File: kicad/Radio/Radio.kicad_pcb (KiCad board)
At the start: 2 copper layers, 129 x 99.5 mm, 44 parts, among them J1 PCB_SMA, J2 Conn_01x02, J3 Audio_Jack, Q1 MOSFET-NCH-AO3404A, Q2 MOSFET-NCH-AO3404A, SW1 Rotary_Encoder_Switch, T1 6:31, T2 31:6, T3 T50_SPLITTER, U1 LM7805_TO220, U2 FST3253, U3 LM358, U4 si5351, U5 TINYPico

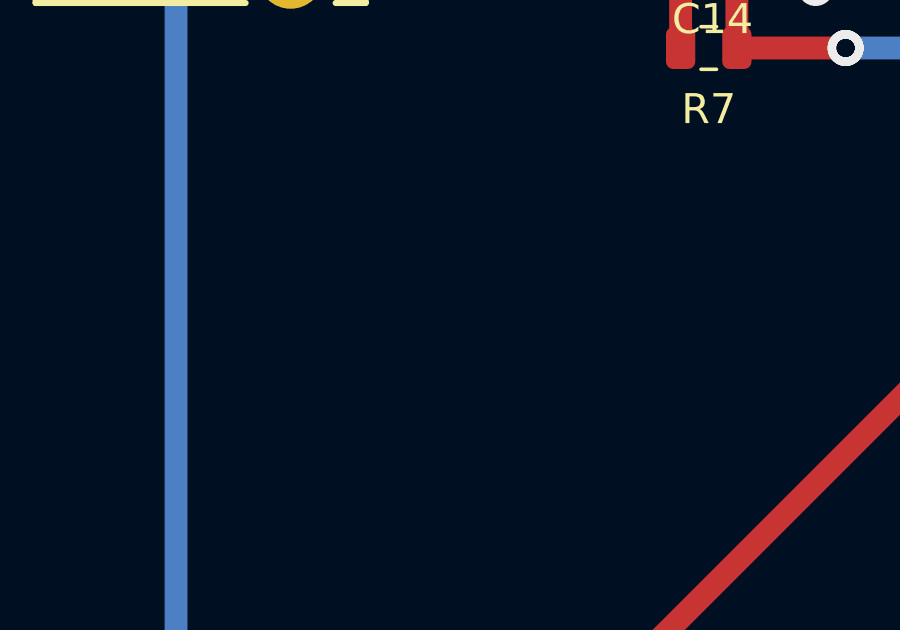
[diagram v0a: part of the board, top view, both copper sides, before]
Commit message: fixing cap placement
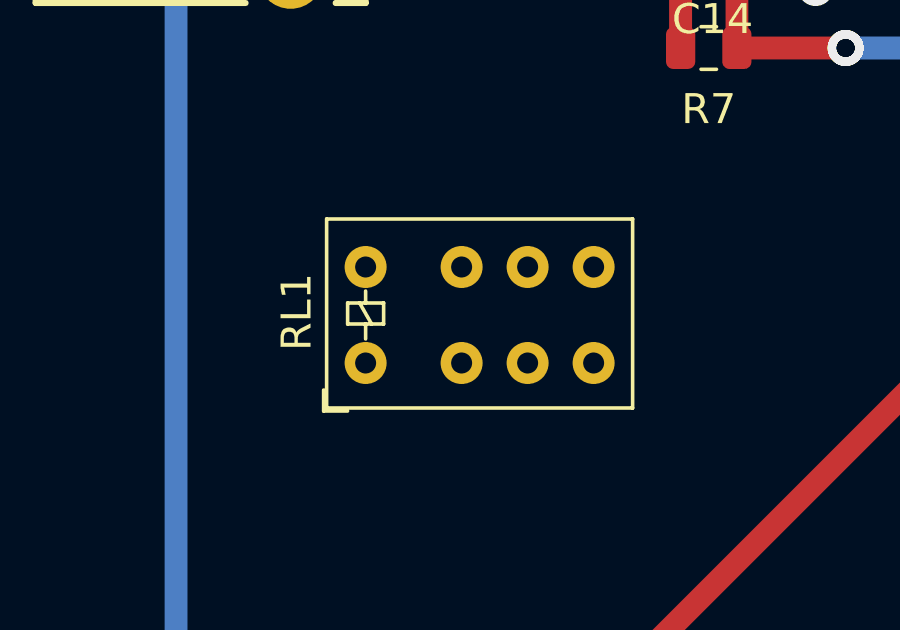
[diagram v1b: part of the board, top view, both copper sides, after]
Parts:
- added RL1: JW2, Relay_THT:Relay_DPDT_AXICOM_IMSeries_Pitch3.2mm, F.Cu at (69.0, 93.5)
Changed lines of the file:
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@@
     (tracks 467)
     (zones 0)
-    (modules 44)
-    (nets 45)
+    (modules 45)
+    (nets 53)
   )
   (page A4)
@@
   (net 43 SCL_HV)
   (net 44 SCL_LV)
+  (net 45 "Net-(RL1-Pad5)")
+  (net 46 "Net-(RL1-Pad6)")
+  (net 47 "Net-(RL1-Pad7)")
+  (net 48 "Net-(RL1-Pad4)")
+  (net 49 "Net-(RL1-Pad3)")
+  (net 50 "Net-(RL1-Pad2)")
+  (net 51 "Net-(RL1-Pad8)")
+  (net 52 "Net-(RL1-Pad1)")
   (net_class Default "This is the default net class."
     (clearance 0.2)
@@
     (add_net "Net-(R4-Pad2)")
     (add_net "Net-(R6-Pad2)")
+    (add_net "Net-(RL1-Pad1)")
+    (add_net "Net-(RL1-Pad2)")
+    (add_net "Net-(RL1-Pad3)")
+    (add_net "Net-(RL1-Pad4)")
+    (add_net "Net-(RL1-Pad5)")
+    (add_net "Net-(RL1-Pad6)")
+    (add_net "Net-(RL1-Pad7)")
+    (add_net "Net-(RL1-Pad8)")
     (add_net "Net-(SW1-PadA)")
     (add_net "Net-(SW1-PadB)")
@@
     (add_net SDA_HV)
     (add_net SDA_LV)
+  )
+  (module Relay_THT:Relay_DPDT_AXICOM_IMSeries_Pitch3.2mm (layer F.Cu)
+    (at 69 93.5 90)
+    (descr "AXICOM IM-Series Relays, DPDR, Pitch 3.2mm, http://www.te.com/commerce/DocumentDelivery/DDEController?Action=showdoc&DocId=Specification+Or+Standard%7F108-98001%7FV%7Fpdf%7FEnglish%7FENG_SS_108-98001_V_IM_0614_v1.pdf%7F4-1462039-1")
+    (tags "AXICOM IM-Series Relay DPDR Pitch 3.2mm")
+    (fp_text reference RL1 (at 1.7 -2.3 90) (layer F.SilkS)
+      (effects (font (size 1 1) (thickness 0.15)))
+    )
+    (fp_text value JW2 (at 1.6 9.9 90) (layer F.Fab)
+      (effects (font (size 1 1) (thickness 0.15)))
+    )
+    (fp_line (start 5.13 9.05) (end -1.85 9.05) (layer F.CrtYd) (width 0.05))
+    (fp_line (start 5.13 9.05) (end 5.13 -1.45) (layer F.CrtYd) (width 0.05))
+    (fp_line (start -1.85 -1.45) (end -1.85 9.05) (layer F.CrtYd) (width 0.05))
+    (fp_line (start -1.85 -1.45) (end 5.13 -1.45) (layer F.CrtYd) (width 0.05))
+    (fp_line (start 4.7 -1.2) (end -1.4 -1.2) (layer F.Fab) (width 0.12))
+    (fp_line (start 4.7 8.8) (end 4.7 -1.2) (layer F.Fab) (width 0.12))
+    (fp_line (start -1.4 8.8) (end 4.7 8.8) (layer F.Fab) (width 0.12))
+    (fp_line (start -1.4 -1.2) (end -1.4 8.8) (layer F.Fab) (width 0.12))
+    (fp_line (start -1.5 -1.3) (end 4.8 -1.3) (layer F.SilkS) (width 0.12))
+    (fp_line (start 4.8 8.9) (end -1.5 8.9) (layer F.SilkS) (width 0.12))
+    (fp_line (start -1.6 -1.4) (end -0.9 -1.4) (layer F.SilkS) (width 0.12))
+    (fp_line (start -1.6 -0.6) (end -1.6 -1.4) (layer F.SilkS) (width 0.12))
+    (fp_line (start 2 -0.6) (end 1.3 -0.6) (layer F.SilkS) (width 0.12))
+    (fp_line (start 2 0.6) (end 2 -0.6) (layer F.SilkS) (width 0.12))
+    (fp_line (start 1.3 0.6) (end 2 0.6) (layer F.SilkS) (width 0.12))
+    (fp_line (start 1.3 -0.6) (end 1.3 0.6) (layer F.SilkS) (width 0.12))
+    (fp_line (start 1.3 0.2) (end 2 -0.2) (layer F.SilkS) (width 0.12))
+    (fp_line (start 1.3 0) (end 0.8 0) (layer F.SilkS) (width 0.12))
+    (fp_line (start 2 0) (end 2.4 0) (layer F.SilkS) (width 0.12))
+    (fp_line (start 0.8 0) (end 2.4 0) (layer F.Fab) (width 0.12))
+    (fp_line (start 4.8 -1.3) (end 4.8 8.9) (layer F.SilkS) (width 0.12))
+    (fp_line (start -1.5 8.9) (end -1.5 -1.3) (layer F.SilkS) (width 0.12))
+    (fp_text user %R (at 1.6 4) (layer F.Fab)
+      (effects (font (size 1 1) (thickness 0.15)))
+    )
+    (pad 5 thru_hole circle (at 3.2 7.6 90) (size 1.4 1.4) (drill 0.7) (layers *.Cu *.Mask)
+      (net 45 "Net-(RL1-Pad5)"))
+    (pad 6 thru_hole circle (at 3.2 5.4 90) (size 1.4 1.4) (drill 0.7) (layers *.Cu *.Mask)
+      (net 46 "Net-(RL1-Pad6)"))
+    (pad 7 thru_hole circle (at 3.2 3.2 90) (size 1.4 1.4) (drill 0.7) (layers *.Cu *.Mask)
+      (net 47 "Net-(RL1-Pad7)"))
+    (pad 4 thru_hole circle (at 0 7.6 90) (size 1.4 1.4) (drill 0.7) (layers *.Cu *.Mask)
+      (net 48 "Net-(RL1-Pad4)"))
+    (pad 3 thru_hole circle (at 0 5.4 90) (size 1.4 1.4) (drill 0.7) (layers *.Cu *.Mask)
+      (net 49 "Net-(RL1-Pad3)"))
+    (pad 2 thru_hole circle (at 0 3.2 90) (size 1.4 1.4) (drill 0.7) (layers *.Cu *.Mask)
+      (net 50 "Net-(RL1-Pad2)"))
+    (pad 8 thru_hole circle (at 3.2 0 90) (size 1.4 1.4) (drill 0.7) (layers *.Cu *.Mask)
+      (net 51 "Net-(RL1-Pad8)"))
+    (pad 1 thru_hole circle (at 0 0 90) (size 1.4 1.4) (drill 0.7) (layers *.Cu *.Mask)
+      (net 52 "Net-(RL1-Pad1)"))
+    (model ${KISYS3DMOD}/Relay_THT.3dshapes/Relay_DPDT_AXICOM_IMSeries_Pitch3.2mm.wrl
+      (at (xyz 0 0 0))
+      (scale (xyz 1 1 1))
+      (rotate (xyz 0 0 0))
+    )
   )
   (module Package_TO_SOT_THT:TO-220-3_Vertical (layer F.Cu)
@@
   (segment (start 82 66) (end 82.5 66.5) (width 0.762) (layer F.Cu) (net 20))
   (segment (start 78.5 66) (end 82 66) (width 0.762) (layer F.Cu) (net 20))
-  (segment (start 109.83 88.862) (end 111 90.032) (width 0.762) (layer B.Cu) (net 42))
-  (segment (start 109.83 87.25) (end 109.83 88.862) (width 0.762) (layer B.Cu) (net 42))
-  (segment (start 111 90.032) (end 111 91) (width 0.762) (layer B.Cu) (net 42))
-  (segment (start 111 91) (end 111 91) (width 0.762) (layer B.Cu) (net 42))
-  (via (at 111 91) (size 1.2) (drill 0.6) (layers F.Cu B.Cu) (net 42))
-  (segment (start 111 91) (end 112.5 92.5) (width 0.762) (layer F.Cu) (net 42))
-  (segment (start 112.5 92.5) (end 146.5 92.5) (width 0.762) (layer F.Cu) (net 42))
-  (segment (start 146.5 92.5) (end 146.5 92.5) (width 0.762) (layer F.Cu) (net 42))
-  (via (at 146.5 92.5) (size 1.2) (drill 0.6) (layers F.Cu B.Cu) (net 42))
-  (segment (start 151.32 92.5) (end 151.5 92.32) (width 0.762) (layer B.Cu) (net 42))
-  (segment (start 146.5 92.5) (end 151.32 92.5) (width 0.762) (layer B.Cu) (net 42))
   (segment (start 117.7 71.31625) (end 115.18375 71.31625) (width 0.762) (layer F.Cu) (net 33))
   (segment (start 115.18375 71.31625) (end 112.5 74) (width 0.762) (layer F.Cu) (net 33))
@@
   (segment (start 126.66 103.66) (end 124 101) (width 0.762) (layer B.Cu) (net 41))
   (segment (start 124 101) (end 123.25 100.25) (width 0.762) (layer B.Cu) (net 41))
+  (segment (start 109.83 88.862) (end 111 90.032) (width 0.762) (layer B.Cu) (net 42))
+  (segment (start 109.83 87.25) (end 109.83 88.862) (width 0.762) (layer B.Cu) (net 42))
+  (segment (start 111 90.032) (end 111 91) (width 0.762) (layer B.Cu) (net 42))
+  (segment (start 111 91) (end 111 91) (width 0.762) (layer B.Cu) (net 42))
+  (via (at 111 91) (size 1.2) (drill 0.6) (layers F.Cu B.Cu) (net 42))
+  (segment (start 111 91) (end 112.5 92.5) (width 0.762) (layer F.Cu) (net 42))
+  (segment (start 112.5 92.5) (end 146.5 92.5) (width 0.762) (layer F.Cu) (net 42))
+  (segment (start 146.5 92.5) (end 146.5 92.5) (width 0.762) (layer F.Cu) (net 42))
+  (via (at 146.5 92.5) (size 1.2) (drill 0.6) (layers F.Cu B.Cu) (net 42))
+  (segment (start 151.32 92.5) (end 151.5 92.32) (width 0.762) (layer B.Cu) (net 42))
+  (segment (start 146.5 92.5) (end 151.32 92.5) (width 0.762) (layer B.Cu) (net 42))
   (segment (start 78.46 122.585) (end 78.5 122.625) (width 0.762) (layer B.Cu) (net 42))
   (segment (start 78.46 118.9375) (end 78.46 122.585) (width 0.762) (layer B.Cu) (net 42))
